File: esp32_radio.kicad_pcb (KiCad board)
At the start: 2 copper layers, 76.2 x 73.7 mm, 37 parts, among them J1 RP-SMA, J2 Adafruit MAX98357, J3 CONN_ADC_EXT, J4 CONN_I2C, U1 ILI9341_TOUCH_SD, U2 RF4IN1, U3 esp32-lolin32, U4 WS2812B, U5 Joystick, U6 Joystick, U7 MCP3008, U8 MAX98357a

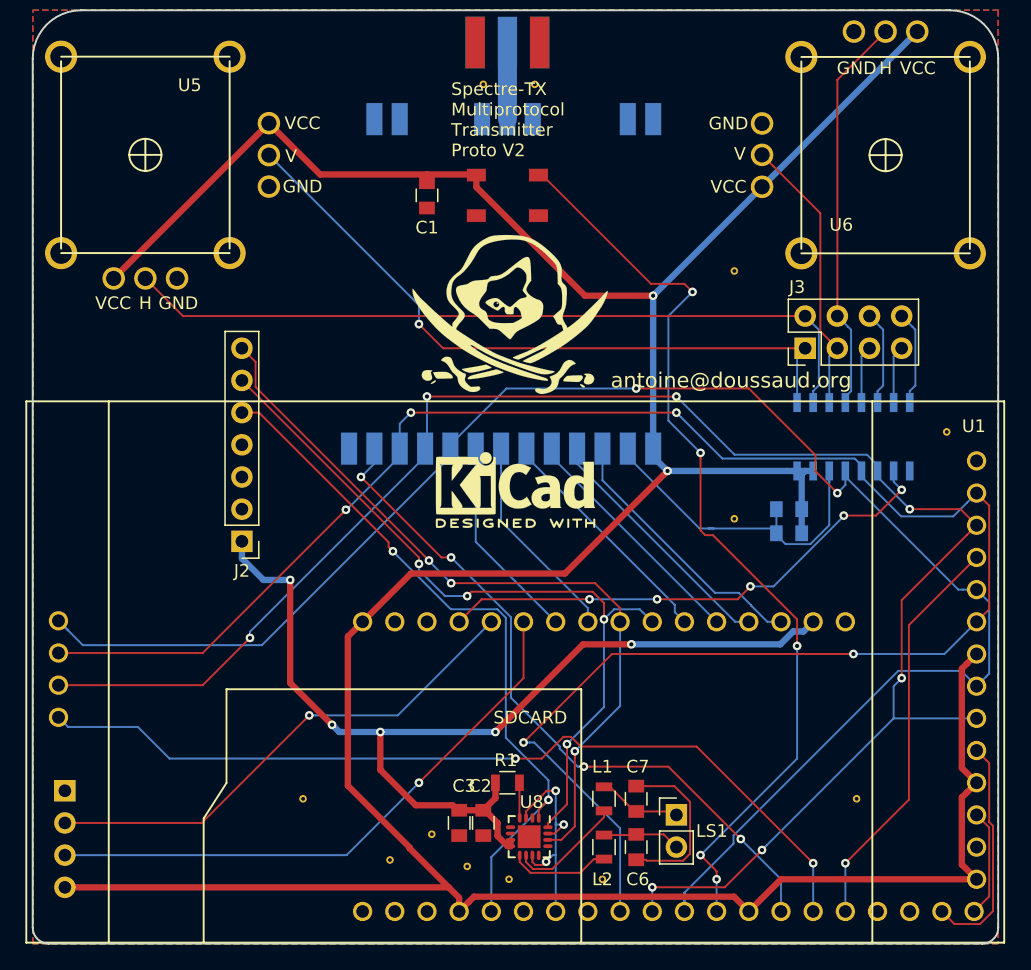
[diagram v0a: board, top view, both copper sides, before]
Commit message: fix nrf24l01 output + remove i2c + working i2s
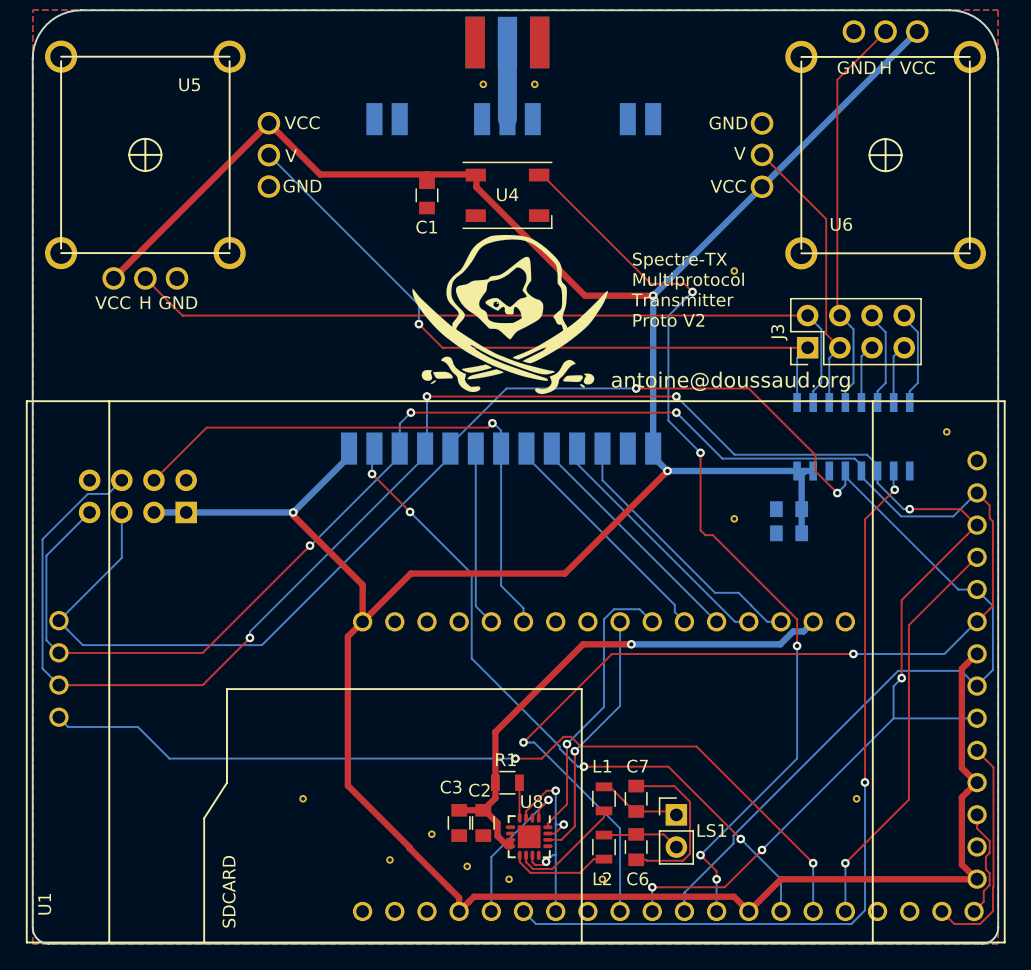
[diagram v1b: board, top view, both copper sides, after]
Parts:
- removed J2: Adafruit MAX98357, Pin_Headers:Pin_Header_Straight_1x07_Pitch2.54mm
- removed J4: CONN_I2C, Pin_Headers:Pin_Header_Straight_1x04_Pitch2.54mm
- removed REF***: KiCad-Logo2_6mm_SilkScreen, Symbols:KiCad-Logo2_6mm_SilkScreen
- added U9: nRF24L01, Pin_Headers:Pin_Header_Straight_2x04_Pitch2.54mm, B.Cu at (121.3, 81.5)
- J3: value CONN_ADC_EXT -> Conn_ADC
- U4: footprint tinkerforge:WS2812B_LED -> LEDs:LED_WS2812B-PLCC4
- moved J3 0.20 mm to (170.4, 68.5)
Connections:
- U2 pad 20: Net-(U2-Pad20) -> +3V3
- U3 pad 31: Net-(U3-Pad31) -> /CS_ADC
- U3 pad 4: /CS_ADC -> Net-(U3-Pad4)
- U3 pad 5: /I2C_SDA -> /CS_CYRF
- U3 pad 6: /I2C_SDL -> /CS_NRF24
- U3 pad 7: /CS_CYRF -> Net-(U3-Pad7)
- U3 pad 8: /CS_NRF24 -> Net-(U3-Pad8)
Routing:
- net /I2C_SDL: track 46.4 -> 0.00 mm, vias 1 -> 0
- net /I2S_DATA: track 55.9 -> 12.4 mm, vias 2 -> 1
- net /I2S_LRC: track 60.8 -> 20.2 mm, vias 3 -> 1
- net /I2C_SDA: track 40.2 -> 0.00 mm, vias 1 -> 0
- net +5V: track 79.9 -> 41.7 mm, vias 5 -> 1
- net /I2S_BCLK: track 60.8 -> 22.8 mm, vias 4 -> 1
- net /CS_NRF24: track 16.5 -> 45.3 mm, vias 0 -> 1
- net GND: track 59.0 -> 32.8 mm
- net /CS_ADC: track 41.0 -> 63.5 mm, vias 5 -> 2
- net /MOSI: track 141.1 -> 161.6 mm
- net /MISO: track 154.2 -> 167.3 mm
- net /SCK: track 135.5 -> 146.4 mm
- net /CS_CYRF: track 16.3 -> 14.2 mm
- net +3V3: track 263.7 -> 262.1 mm, vias 2 -> 3
- net /EXT_ADC_CH3: track 31.5 -> 32.1 mm
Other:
- board text removed: "3.3V"
- board text removed: "GND"
- board text removed: "SDA"
- board text removed: "SDL"

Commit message: osh v3
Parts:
- removed G***: LOGO, spectre:Logo
- removed the REF** at (130.6, 104.1)
- removed the REF** at (154.2, 110.5)
- removed the REF** at (140.7, 106.9)
- removed the REF** at (137.4, 109.0)
- removed the REF** at (181.4, 75.2)
- removed the REF** at (174.2, 104.1)
- removed the REF** at (164.6, 62.5)
- removed the REF** at (164.6, 82.0)
- removed the REF** at (148.8, 47.8)
- removed the REF** at (144.8, 47.8)
- removed the REF** at (143.5, 109.5)
- removed the REF** at (146.8, 110.5)
- added REF**: Via, spectre:Via, F.Cu at (173.5, 86.0)
- added REF**: Via, spectre:Via, F.Cu at (138.8, 104.2)
- added REF**: Via, spectre:Via, F.Cu at (154.5, 70.0)
- added REF**: Via, spectre:Via, F.Cu at (158.8, 103.2)
- added REF**: Via, spectre:Via, F.Cu at (142.0, 62.2)
- added REF**: Via, spectre:Via, F.Cu at (140.8, 104.2)
- added REF**: Via, spectre:Via, F.Cu at (138.8, 103.2)
- added REF**: Via, spectre:Via, F.Cu at (139.8, 102.2)
- added REF**: Via, spectre:Via, F.Cu at (166.8, 98.2)
- added REF**: Via, spectre:Via, F.Cu at (140.8, 103.2)
- added REF**: Via, spectre:Via, F.Cu at (165.8, 98.2)
- added REF**: Via, spectre:Via, F.Cu at (167.8, 98.2)
- added REF**: Via, spectre:Via, F.Cu at (139.8, 103.2)
- added REF**: Via, spectre:Via, F.Cu at (173.5, 88.0)
- added REF**: Via, spectre:Via, F.Cu at (172.5, 85.0)
- added REF**: Via, spectre:Via, F.Cu at (172.5, 86.0)
- added REF**: Via, spectre:Via, F.Cu at (172.5, 88.0)
- added REF**: Via, spectre:Via, F.Cu at (173.5, 87.0)
- added REF**: Via, spectre:Via, F.Cu at (172.5, 87.0)
- added REF**: Via, spectre:Via, F.Cu at (167.8, 96.2)
- added REF**: Via, spectre:Via, F.Cu at (167.8, 97.2)
- added REF**: Via, spectre:Via, F.Cu at (166.8, 97.2)
- added REF**: Via, spectre:Via, F.Cu at (165.8, 97.2)
- added REF**: Via, spectre:Via, F.Cu at (167.8, 95.2)
- added REF**: Via, spectre:Via, F.Cu at (166.8, 96.2)
- added REF**: Via, spectre:Via, F.Cu at (173.5, 85.0)
- added REF**: Via, spectre:Via, F.Cu at (137.8, 102.2)
- added REF**: Via, spectre:Via, F.Cu at (137.8, 103.2)
- added REF**: Via, spectre:Via, F.Cu at (137.8, 104.2)
- added REF**: Via, spectre:Via, F.Cu at (170.5, 88.0)
- added REF**: Via, spectre:Via, F.Cu at (170.5, 87.0)
- added REF**: Via, spectre:Via, F.Cu at (171.5, 88.0)
- added REF**: Via, spectre:Via, F.Cu at (170.5, 86.0)
- added REF**: Via, spectre:Via, F.Cu at (170.5, 85.0)
- added REF**: Via, spectre:Via, F.Cu at (171.5, 87.0)
- added REF**: Via, spectre:Via, F.Cu at (171.5, 86.0)
- added REF**: Via, spectre:Via, F.Cu at (165.8, 96.2)
- added REF**: Via, spectre:Via, F.Cu at (171.5, 85.0)
- added REF**: Via, spectre:Via, F.Cu at (129.2, 106.8)
- added REF**: Via, spectre:Via, F.Cu at (128.2, 106.8)
- added REF**: Via, spectre:Via, F.Cu at (127.2, 106.8)
- added REF**: Via, spectre:Via, F.Cu at (126.2, 106.8)
- added REF**: Via, spectre:Via, F.Cu at (125.2, 106.8)
- added REF**: Via, spectre:Via, F.Cu at (124.2, 106.8)
- added REF**: Via, spectre:Via, F.Cu at (162.2, 57.2)
- added REF**: Via, spectre:Via, F.Cu at (161.2, 57.2)
- added REF**: Via, spectre:Via, F.Cu at (160.2, 57.2)
- added REF**: Via, spectre:Via, F.Cu at (166.8, 95.2)
- added REF**: Via, spectre:Via, F.Cu at (159.2, 57.2)
- added REF**: Via, spectre:Via, F.Cu at (158.2, 57.2)
- added REF**: Via, spectre:Via, F.Cu at (157.2, 57.2)
- added REF**: Via, spectre:Via, F.Cu at (156.2, 57.2)
- added REF**: Via, spectre:Via, F.Cu at (155.2, 57.2)
- added REF**: Via, spectre:Via, F.Cu at (147.0, 64.2)
- added REF**: Via, spectre:Via, F.Cu at (146.0, 64.2)
- added REF**: Via, spectre:Via, F.Cu at (145.0, 64.2)
- added REF**: Via, spectre:Via, F.Cu at (144.0, 64.2)
- added REF**: Via, spectre:Via, F.Cu at (143.0, 64.2)
- added REF**: Via, spectre:Via, F.Cu at (165.8, 95.2)
- added REF**: Via, spectre:Via, F.Cu at (142.0, 64.2)
- added REF**: Via, spectre:Via, F.Cu at (129.2, 105.8)
- added REF**: Via, spectre:Via, F.Cu at (128.2, 105.8)
- added REF**: Via, spectre:Via, F.Cu at (127.2, 105.8)
- added REF**: Via, spectre:Via, F.Cu at (126.2, 105.8)
- added REF**: Via, spectre:Via, F.Cu at (125.2, 105.8)
- added REF**: Via, spectre:Via, F.Cu at (124.2, 105.8)
- added REF**: Via, spectre:Via, F.Cu at (162.2, 56.2)
- added REF**: Via, spectre:Via, F.Cu at (161.2, 56.2)
- added REF**: Via, spectre:Via, F.Cu at (160.2, 56.2)
- added REF**: Via, spectre:Via, F.Cu at (140.8, 102.2)
- added REF**: Via, spectre:Via, F.Cu at (159.2, 56.2)
- added REF**: Via, spectre:Via, F.Cu at (158.2, 56.2)
- added REF**: Via, spectre:Via, F.Cu at (157.2, 56.2)
- added REF**: Via, spectre:Via, F.Cu at (156.2, 56.2)
- added REF**: Via, spectre:Via, F.Cu at (155.2, 56.2)
- added REF**: Via, spectre:Via, F.Cu at (147.0, 63.2)
- added REF**: Via, spectre:Via, F.Cu at (146.0, 63.2)
- added REF**: Via, spectre:Via, F.Cu at (145.0, 63.2)
- added REF**: Via, spectre:Via, F.Cu at (144.0, 63.2)
- added REF**: Via, spectre:Via, F.Cu at (143.0, 63.2)
- added REF**: Via, spectre:Via, F.Cu at (138.8, 102.2)
- added REF**: Via, spectre:Via, F.Cu at (142.0, 63.2)
- added REF**: Via, spectre:Via, F.Cu at (129.2, 104.8)
- added REF**: Via, spectre:Via, F.Cu at (128.2, 104.8)
- added REF**: Via, spectre:Via, F.Cu at (127.2, 104.8)
- added REF**: Via, spectre:Via, F.Cu at (126.2, 104.8)
- added REF**: Via, spectre:Via, F.Cu at (125.2, 104.8)
- added REF**: Via, spectre:Via, F.Cu at (124.2, 104.8)
- added REF**: Via, spectre:Via, F.Cu at (162.2, 55.2)
- added REF**: Via, spectre:Via, F.Cu at (161.2, 55.2)
- added REF**: Via, spectre:Via, F.Cu at (160.2, 55.2)
- added REF**: Via, spectre:Via, F.Cu at (139.8, 104.2)
- added REF**: Via, spectre:Via, F.Cu at (159.2, 55.2)
- added REF**: Via, spectre:Via, F.Cu at (158.2, 55.2)
- added REF**: Via, spectre:Via, F.Cu at (157.2, 55.2)
- added REF**: Via, spectre:Via, F.Cu at (156.2, 55.2)
- added REF**: Via, spectre:Via, F.Cu at (155.2, 55.2)
- added REF**: Via, spectre:Via, F.Cu at (147.0, 62.2)
- added REF**: Via, spectre:Via, F.Cu at (146.0, 62.2)
- added REF**: Via, spectre:Via, F.Cu at (145.0, 62.2)
- added REF**: Via, spectre:Via, F.Cu at (144.0, 62.2)
- added REF**: Via, spectre:Via, F.Cu at (143.0, 62.2)
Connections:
- net Net-(U3-Pad3) renamed /INT_ADC_CH0
- net Net-(U3-Pad4) renamed /INT_ADC_CH1
- net Net-(U3-Pad7) renamed /INT_ADC_CH2
- net Net-(U3-Pad8) renamed /INT_ADC_CH3
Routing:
- net GND: track 32.8 -> 44.3 mm, vias 3 -> 6
- net /SCK: track 146.4 -> 143.8 mm
- net /MOSI: track 161.6 -> 159.6 mm
- net /MISO: track 167.3 -> 168.1 mm
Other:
- rule pad_to_mask_clearance: 0.2 -> 0.0508

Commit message: osh v3
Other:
- board text added: "Spectre-TX Multiprotocol Transmitter Proto V3"
- board text removed: "Spectre-TX Multiprotocol Transmitter Proto V2"
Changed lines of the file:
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@@
     (arrow2b (pts (xy 109.22 124.46) (xy 110.346504 123.873579)))
   )
-  (gr_text "Spectre-TX\nMultiprotocol\nTransmitter\nProto V2" (at 156.5 64) (layer F.SilkS)
+  (gr_text "Spectre-TX\nMultiprotocol\nTransmitter\nProto V3" (at 156.5 64) (layer F.SilkS)
     (effects (font (size 1 1) (thickness 0.2)) (justify left))
   )

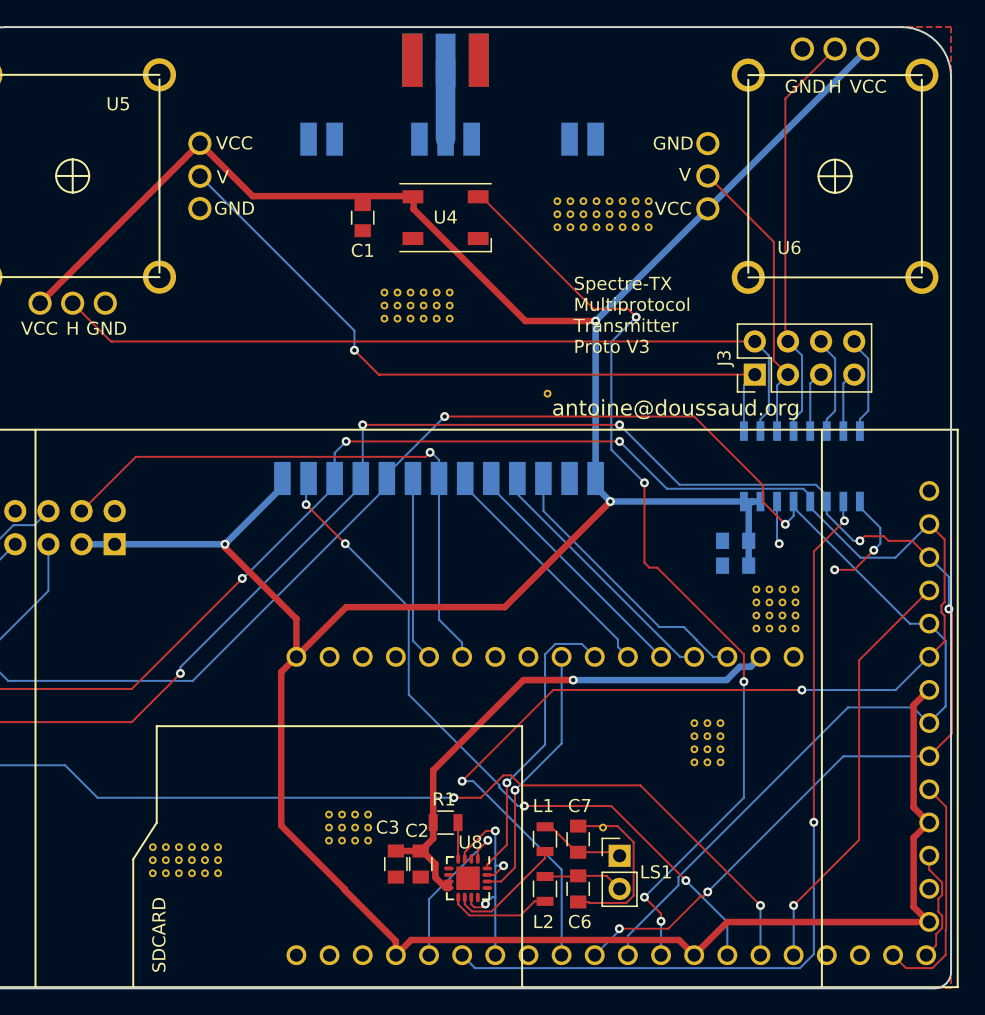
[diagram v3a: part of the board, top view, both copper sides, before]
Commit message: fix mosi near edge + fix nrf24 shematic + fix RF4in1 footprint
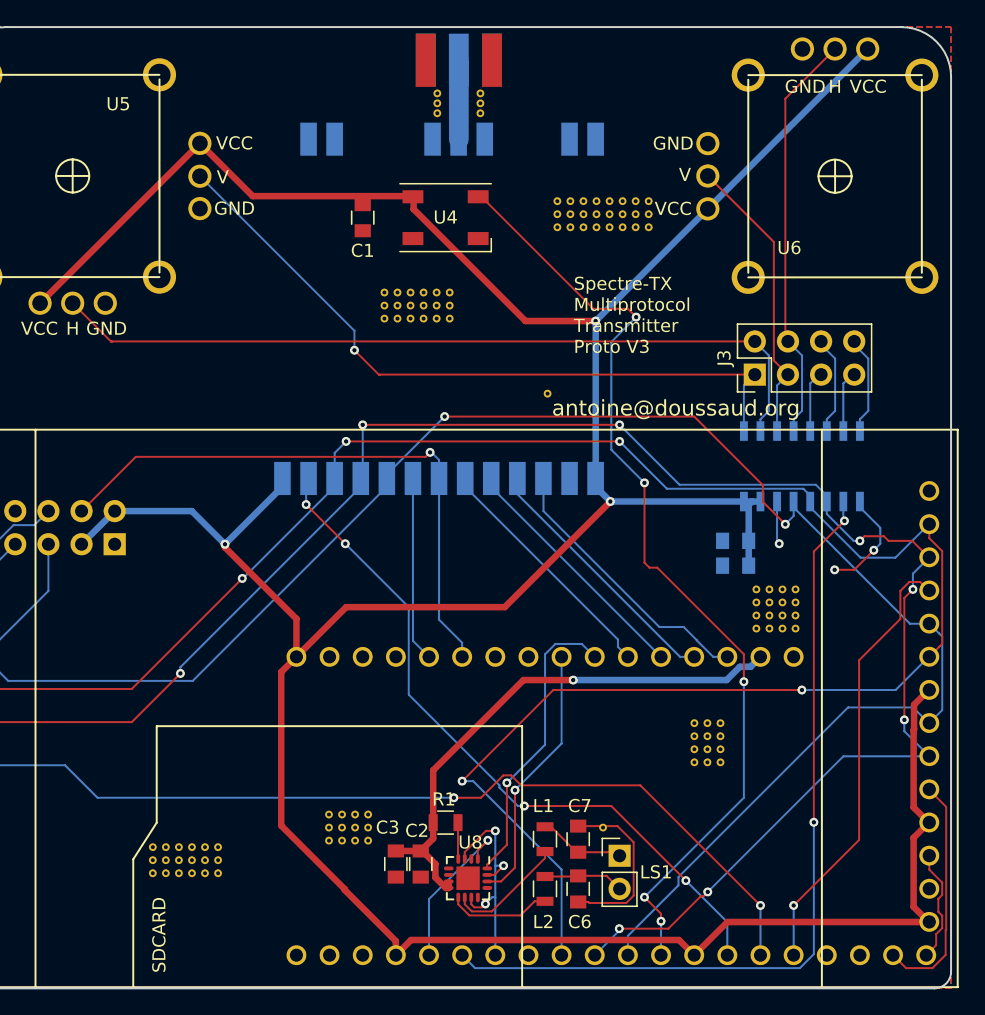
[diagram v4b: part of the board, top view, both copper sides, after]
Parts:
- added REF**: Via, spectre:Via, F.Cu at (146.1, 47.0)
- added REF**: Via, spectre:Via, F.Cu at (146.1, 47.8)
- added REF**: Via, spectre:Via, F.Cu at (146.1, 48.5)
- added REF**: Via, spectre:Via, F.Cu at (149.4, 47.0)
- added REF**: Via, spectre:Via, F.Cu at (149.4, 47.8)
- added REF**: Via, spectre:Via, F.Cu at (149.4, 48.5)
- moved J1 1.02 mm to (147.7, 44.5)
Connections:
- U9 pad 1: +3V3 -> GND
- U9 pad 2: GND -> +3V3
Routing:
- net +3V3: track 262.1 -> 264.2 mm
- net /CS_TOUCH: track 32.2 -> 34.0 mm
- net /MOSI: track 159.6 -> 159.7 mm, vias 7 -> 8

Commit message: v4
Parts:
- U9: footprint Pin_Headers:Pin_Header_Straight_2x04_Pitch2.54mm -> RF_Modules:nRF24L01_Breakout
- moved U9 1.86 mm to (123.2, 81.5)
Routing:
- net /MOSI: track 159.7 -> 161.5 mm
- net /MISO: track 167.7 -> 169.6 mm
- net +3V3: track 264.2 -> 262.4 mm
- net /CS_NRF24: track 45.3 -> 44.5 mm
- net /SCK: track 143.6 -> 144.4 mm
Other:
- board text added: "Spectre-TX Multiprotocol Transmitter Proto V4"
- board text removed: "Spectre-TX Multiprotocol Transmitter Proto V3"
